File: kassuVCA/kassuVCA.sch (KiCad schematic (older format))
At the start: 20 parts, among them J1 Conn_02x05_Odd_Even, Q1 2N3904, Q2 2N3904, Q3 2N3904, U1 TL072

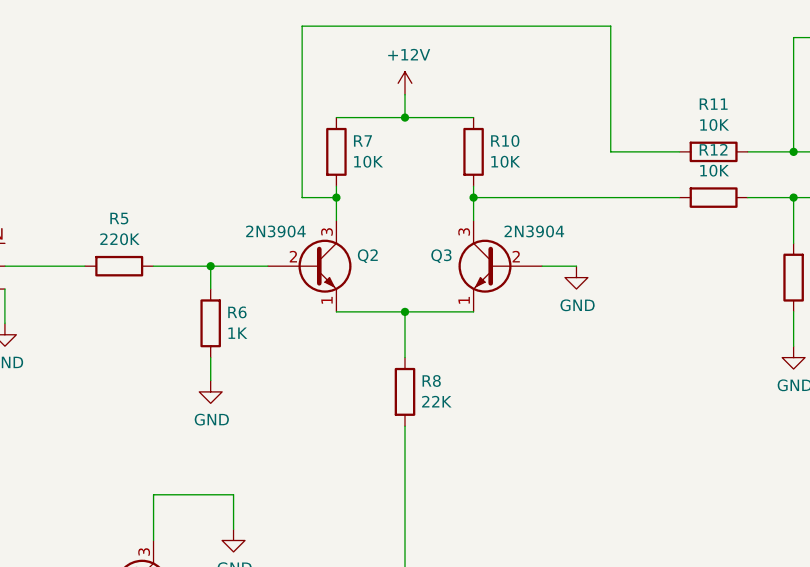
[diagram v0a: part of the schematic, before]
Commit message: switch to mbt3904 double transistor 2n3904 dual package
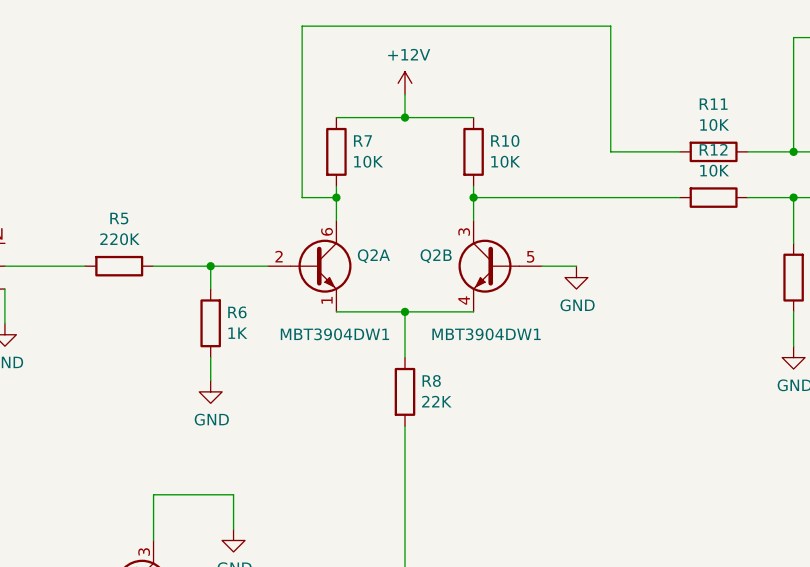
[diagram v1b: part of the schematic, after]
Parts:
- removed Q2, Q3: 2N3904, Package_TO_SOT_THT:TO-92L_Inline_Wide, symbol Transistor_BJT:2N3904
- added Q2: MBT3904DW1, Package_TO_SOT_SMD:SOT-363_SC-70-6, symbol Transistor_BJT:MBT3904DW1
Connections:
- net GND: now also Q2.5 (B2)
- net at R8.1: now also Q2.1 (E1), Q2.4 (E2)
- net at R5.1, R6.2: now also Q2.2 (B1)
- net at R11.2, R7.2: now also Q2.6 (C1)
- net at R10.2, R12.2: now also Q2.3 (C2)
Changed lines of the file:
@@
 $EndDescr
-$Comp
-L Transistor_BJT:2N3904 Q2
-U 1 1 622D83A3
-P 4100 2200
-F 0 "Q2" H 4290 2246 50  0000 L CNN
-F 1 "2N3904" H 3800 2350 50  0000 L CNN
-F 2 "Package_TO_SOT_THT:TO-92L_Inline_Wide" H 4300 2125 50  0001 L CIN
-F 3 "https://www.onsemi.com/pub/Collateral/2N3903-D.PDF" H 4100 2200 50  0001 L CNN
-	1    4100 2200
-	1    0    0    -1
-$EndComp
-$Comp
-L Transistor_BJT:2N3904 Q3
-U 1 1 622D8CF8
-P 4900 2200
-F 0 "Q3" H 5091 2246 50  0000 L CNN
-F 1 "2N3904" H 4600 2350 50  0000 L CNN
-F 2 "Package_TO_SOT_THT:TO-92L_Inline_Wide" H 5100 2125 50  0001 L CIN
-F 3 "https://www.onsemi.com/pub/Collateral/2N3903-D.PDF" H 4900 2200 50  0001 L CNN
-	1    4900 2200
-	-1   0    0    -1
-$EndComp
 $Comp
 L Transistor_BJT:2N3904 Q1
@@
 	1    0    0    -1
 $EndComp
+$Comp
+L Transistor_BJT:MBT3904DW1 Q2
+U 1 1 6229C328
+P 4100 2200
+F 0 "Q2" H 4290 2246 50  0000 L CNN
+F 1 "MBT3904DW1" H 3950 1900 50  0000 L CNN
+F 2 "Package_TO_SOT_SMD:SOT-363_SC-70-6" H 4300 2300 50  0001 C CNN
+F 3 "http://www.onsemi.com/pub_link/Collateral/MBT3904DW1T1-D.PDF" H 4100 2200 50  0001 C CNN
+	1    4100 2200
+	1    0    0    -1
+$EndComp
+$Comp
+L Transistor_BJT:MBT3904DW1 Q2
+U 2 1 6229CF49
+P 4900 2200
+F 0 "Q2" H 5091 2246 50  0000 L CNN
+F 1 "MBT3904DW1" H 4700 1900 50  0000 L CNN
+F 2 "Package_TO_SOT_SMD:SOT-363_SC-70-6" H 5100 2300 50  0001 C CNN
+F 3 "http://www.onsemi.com/pub_link/Collateral/MBT3904DW1T1-D.PDF" H 4900 2200 50  0001 C CNN
+	2    4900 2200
+	-1   0    0    -1
+$EndComp
 $EndSCHEMATC

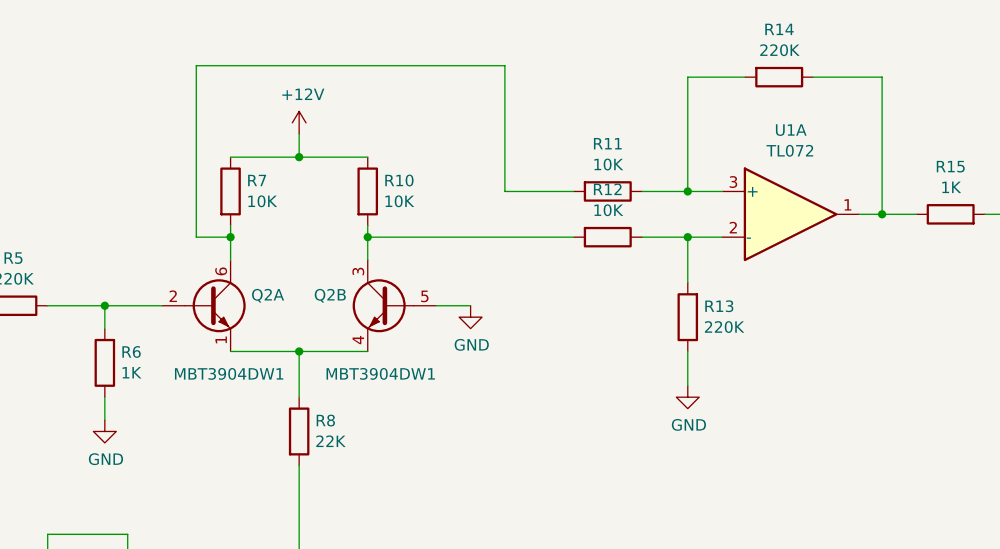
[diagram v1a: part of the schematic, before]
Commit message: VCA state working with jelly bean 2n3904 transistors
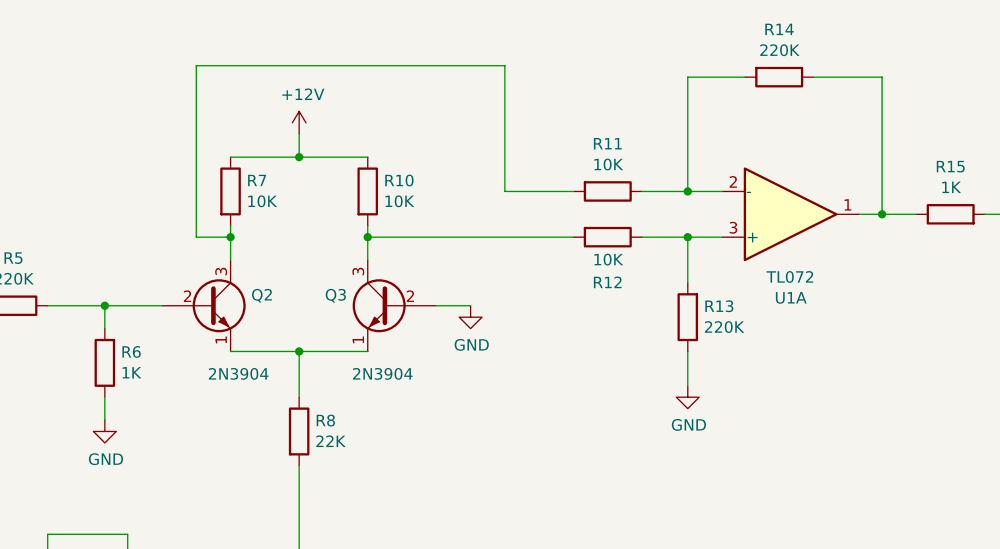
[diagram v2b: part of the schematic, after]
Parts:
- removed Q2: MBT3904DW1, Package_TO_SOT_SMD:SOT-363_SC-70-6, symbol Transistor_BJT:MBT3904DW1
- added Q2, Q3: 2N3904, Package_TO_SOT_THT:TO-92L_Inline_Wide, symbol Transistor_BJT:2N3904
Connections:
- net GND: now also Q3.2 (B)
- net at R12.1, R13.2: now also U1.3 (+); no longer U1.2 (-)
- net at R11.1, R14.2: now also U1.2 (-); no longer U1.3 (+)
- net at R8.1: now also Q2.1 (E), Q3.1 (E)
- net at R5.1, R6.2: now also Q2.2 (B)
- net at R11.2, R7.2: now also Q2.3 (C)
- net at R10.2, R12.2: now also Q3.3 (C)
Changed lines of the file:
@@
 	4500 2600 4500 2400
 Connection ~ 4500 2400
-Wire Wire Line
-	4500 2400 4800 2400
 $Comp
 L power:GND #PWR0106
@@
 U 1 1 62321712
 P 5850 1900
-F 0 "R12" V 5643 1900 50  0000 C CNN
-F 1 "10K" V 5734 1900 50  0000 C CNN
+F 0 "R12" V 6050 1900 50  0000 C CNN
+F 1 "10K" V 5950 1900 50  0000 C CNN
 F 2 "Resistor_THT:R_Axial_DIN0207_L6.3mm_D2.5mm_P10.16mm_Horizontal" V 5780 1900 50  0001 C CNN
 F 3 "~" H 5850 1900 50  0001 C CNN
@@
 F 3 "http://www.ti.com/lit/ds/symlink/tl071.pdf" H 6650 1800 50  0001 C CNN
 	1    6650 1800
-	1    0    0    -1
+	1    0    0    1
 $EndComp
 $Comp
@@
 $EndComp
 $Comp
-L Transistor_BJT:MBT3904DW1 Q2
-U 1 1 6229C328
+L Transistor_BJT:2N3904 Q2
+U 1 1 623E074C
 P 4100 2200
 F 0 "Q2" H 4290 2246 50  0000 L CNN
-F 1 "MBT3904DW1" H 3950 1900 50  0000 L CNN
-F 2 "Package_TO_SOT_SMD:SOT-363_SC-70-6" H 4300 2300 50  0001 C CNN
-F 3 "http://www.onsemi.com/pub_link/Collateral/MBT3904DW1T1-D.PDF" H 4100 2200 50  0001 C CNN
+F 1 "2N3904" H 4100 1900 50  0000 L CNN
+F 2 "Package_TO_SOT_THT:TO-92L_Inline_Wide" H 4300 2125 50  0001 L CIN
+F 3 "https://www.onsemi.com/pub/Collateral/2N3903-D.PDF" H 4100 2200 50  0001 L CNN
 	1    4100 2200
 	1    0    0    -1
 $EndComp
 $Comp
-L Transistor_BJT:MBT3904DW1 Q2
-U 2 1 6229CF49
+L Transistor_BJT:2N3904 Q3
+U 1 1 623E0DE4
 P 4900 2200
-F 0 "Q2" H 5091 2246 50  0000 L CNN
-F 1 "MBT3904DW1" H 4700 1900 50  0000 L CNN
-F 2 "Package_TO_SOT_SMD:SOT-363_SC-70-6" H 5100 2300 50  0001 C CNN
-F 3 "http://www.onsemi.com/pub_link/Collateral/MBT3904DW1T1-D.PDF" H 4900 2200 50  0001 C CNN
-	2    4900 2200
+F 0 "Q3" H 5090 2246 50  0000 L CNN
+F 1 "2N3904" H 4800 1900 50  0000 L CNN
+F 2 "Package_TO_SOT_THT:TO-92L_Inline_Wide" H 5100 2125 50  0001 L CIN
+F 3 "https://www.onsemi.com/pub/Collateral/2N3903-D.PDF" H 4900 2200 50  0001 L CNN
+	1    4900 2200
 	-1   0    0    -1
 $EndComp
+Wire Wire Line
+	4500 2400 4800 2400
 $EndSCHEMATC

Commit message: mini transistor success!
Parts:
- removed Q2, Q3: 2N3904, Package_TO_SOT_THT:TO-92L_Inline_Wide, symbol Transistor_BJT:2N3904
- added Q2: MBT3904DW1, Package_TO_SOT_SMD:SOT-363_SC-70-6, symbol Transistor_BJT:MBT3904DW1
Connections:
- net GND: now also Q2.5 (B2)
- net at R11.2, R7.2: now also Q2.6 (C1)
- net at R10.2, R12.2: now also Q2.3 (C2)
- net at R8.1: now also Q2.1 (E1), Q2.4 (E2)
- net at R5.1, R6.2: now also Q2.2 (B1)
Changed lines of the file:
@@
 	1    0    0    -1
 $EndComp
+Wire Wire Line
+	4500 2400 4800 2400
 $Comp
-L Transistor_BJT:2N3904 Q2
-U 1 1 623E074C
+L Transistor_BJT:MBT3904DW1 Q2
+U 1 1 624028ED
 P 4100 2200
 F 0 "Q2" H 4290 2246 50  0000 L CNN
-F 1 "2N3904" H 4100 1900 50  0000 L CNN
-F 2 "Package_TO_SOT_THT:TO-92L_Inline_Wide" H 4300 2125 50  0001 L CIN
-F 3 "https://www.onsemi.com/pub/Collateral/2N3903-D.PDF" H 4100 2200 50  0001 L CNN
+F 1 "MBT3904DW1" H 3950 1900 50  0000 L CNN
+F 2 "Package_TO_SOT_SMD:SOT-363_SC-70-6" H 4300 2300 50  0001 C CNN
+F 3 "http://www.onsemi.com/pub_link/Collateral/MBT3904DW1T1-D.PDF" H 4100 2200 50  0001 C CNN
 	1    4100 2200
 	1    0    0    -1
 $EndComp
 $Comp
-L Transistor_BJT:2N3904 Q3
-U 1 1 623E0DE4
+L Transistor_BJT:MBT3904DW1 Q2
+U 2 1 62403809
 P 4900 2200
-F 0 "Q3" H 5090 2246 50  0000 L CNN
-F 1 "2N3904" H 4800 1900 50  0000 L CNN
-F 2 "Package_TO_SOT_THT:TO-92L_Inline_Wide" H 5100 2125 50  0001 L CIN
-F 3 "https://www.onsemi.com/pub/Collateral/2N3903-D.PDF" H 4900 2200 50  0001 L CNN
-	1    4900 2200
+F 0 "Q2" H 5091 2246 50  0000 L CNN
+F 1 "MBT3904DW1" H 4700 1900 50  0000 L CNN
+F 2 "Package_TO_SOT_SMD:SOT-363_SC-70-6" H 5100 2300 50  0001 C CNN
+F 3 "http://www.onsemi.com/pub_link/Collateral/MBT3904DW1T1-D.PDF" H 4900 2200 50  0001 C CNN
+	2    4900 2200
 	-1   0    0    -1
 $EndComp
-Wire Wire Line
-	4500 2400 4800 2400
 $EndSCHEMATC

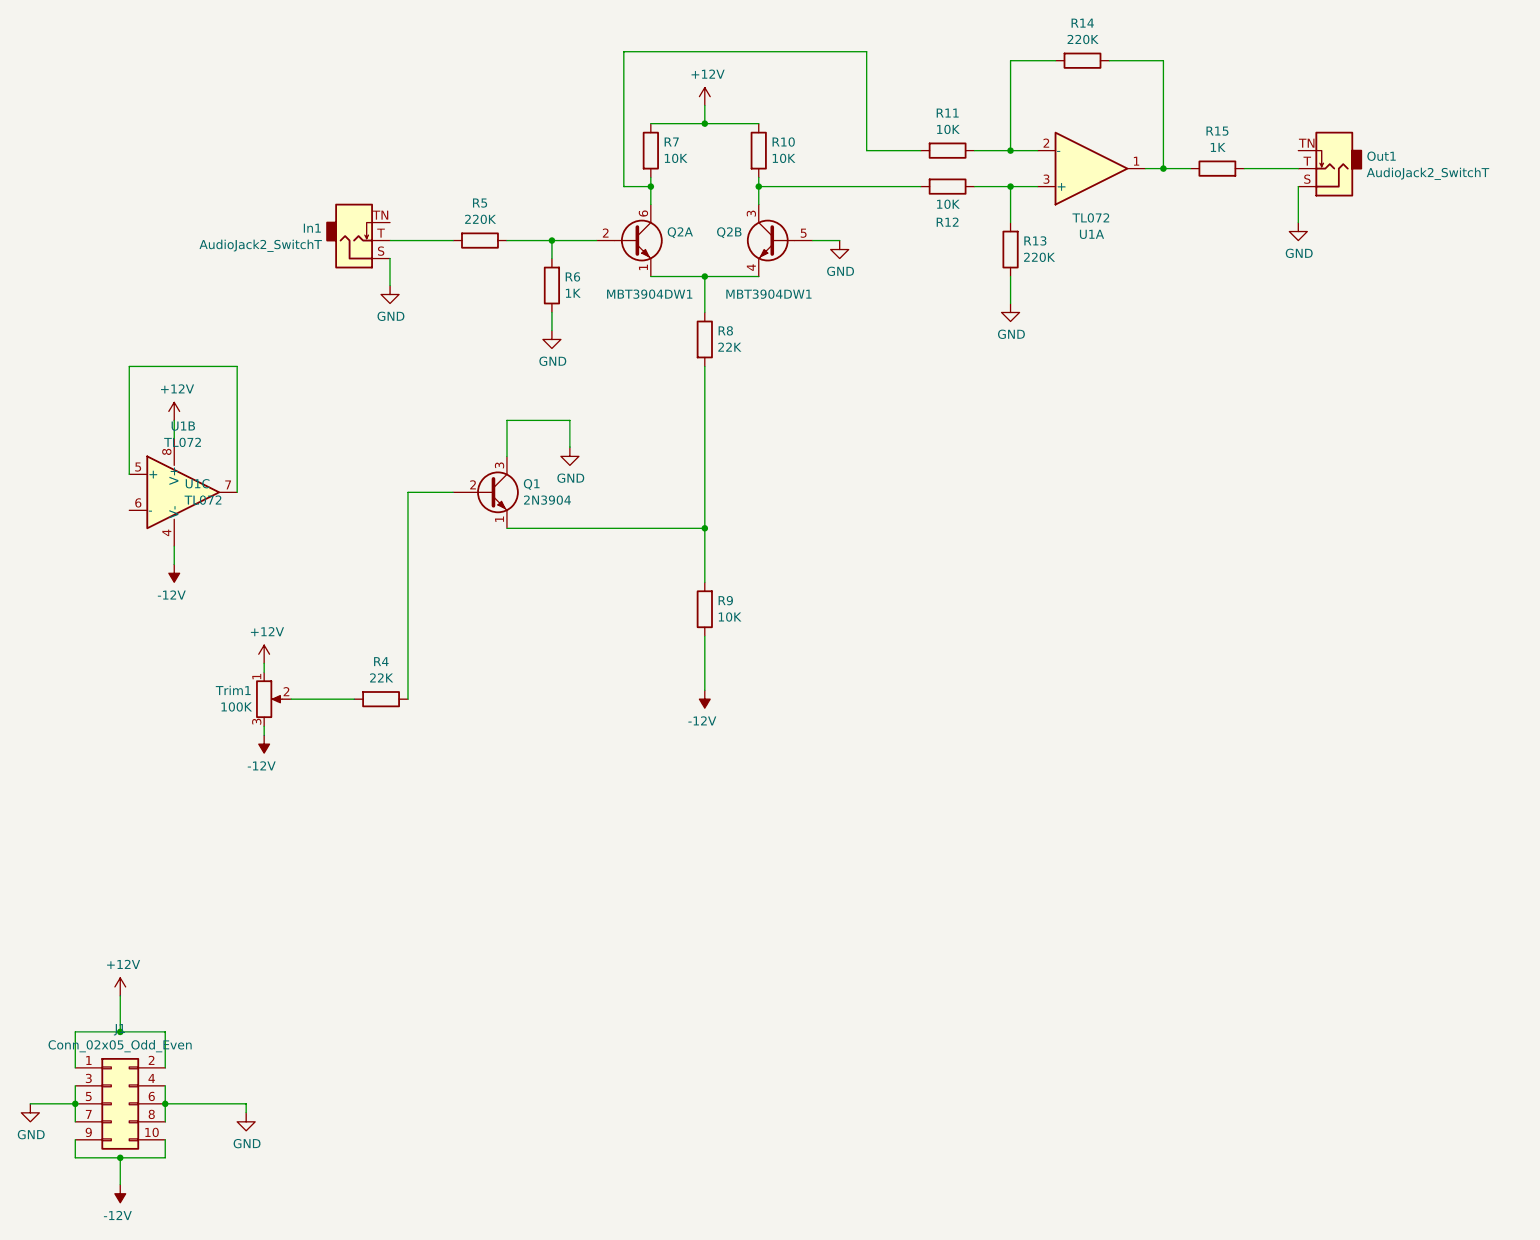
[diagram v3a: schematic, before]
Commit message: WIP working towards a mixer
2 channels laid out with 207 resistors and TL074s. I need to move to TL072s and monolithic transistors in a few places for saner routing
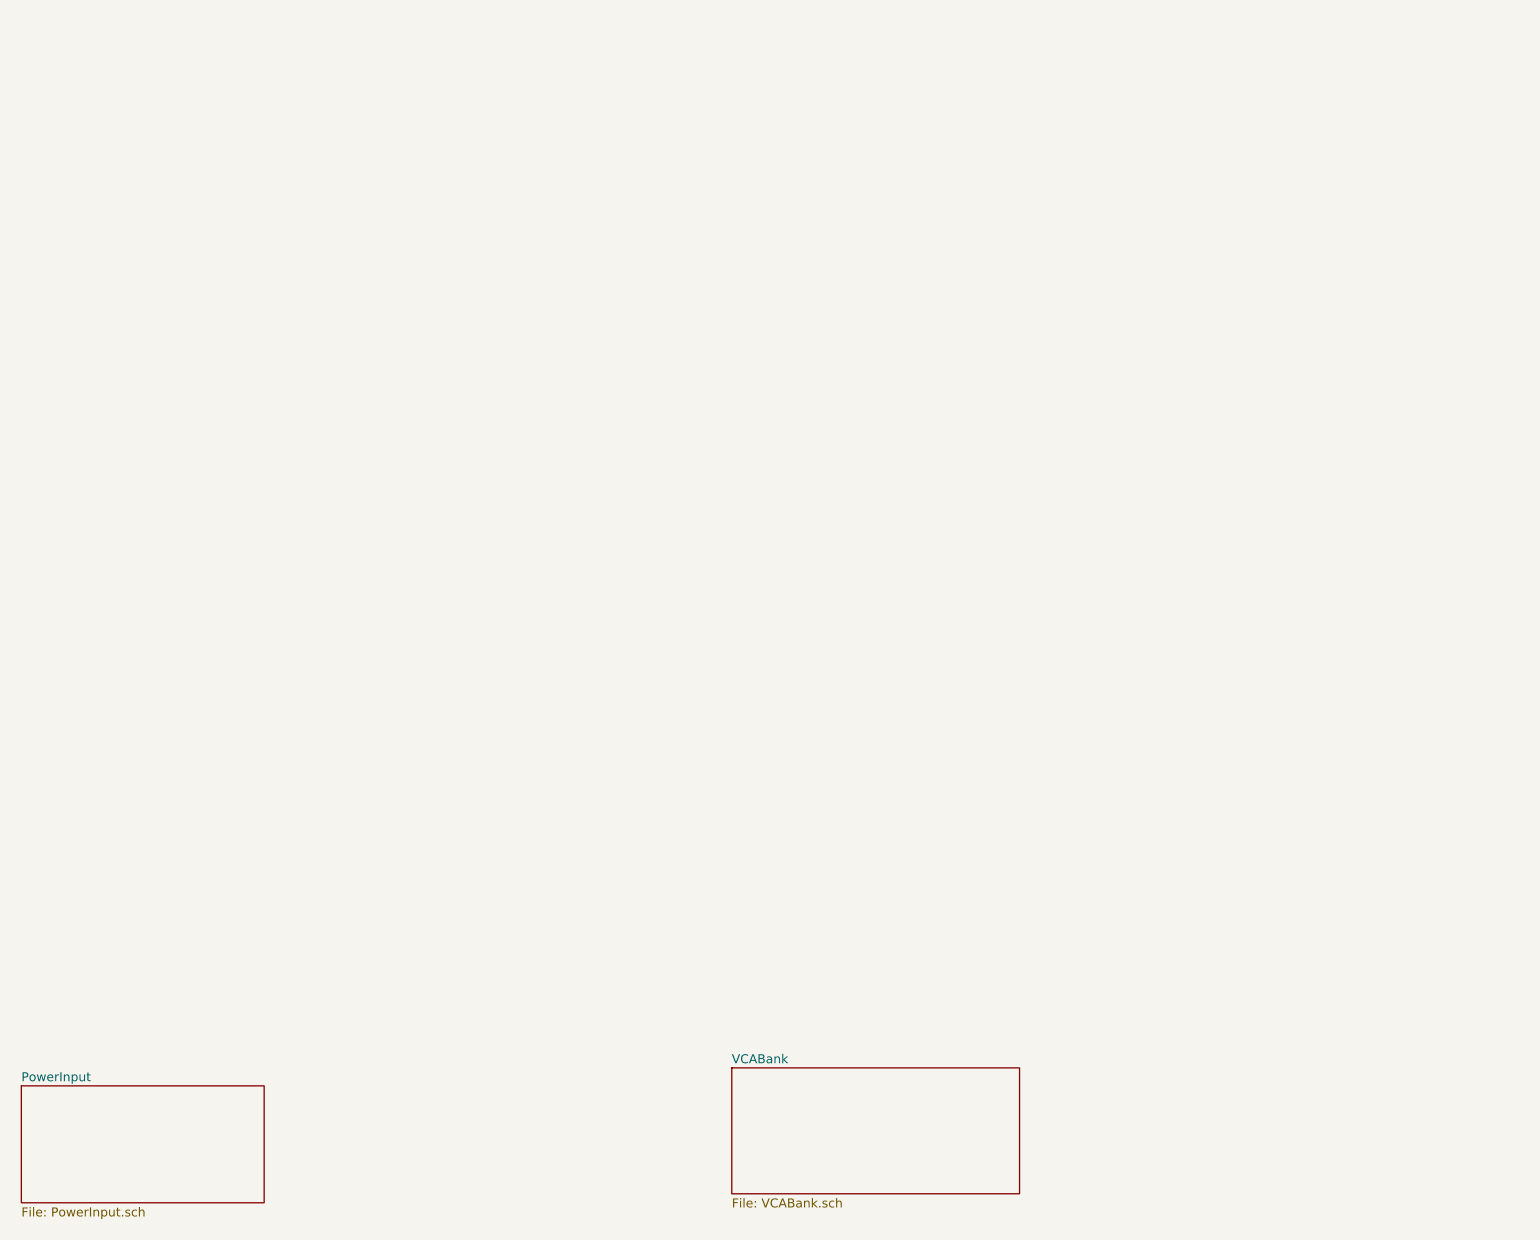
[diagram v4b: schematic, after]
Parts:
- removed In1, Out1: AudioJack2_SwitchT, Connector_Audio:Jack_3.5mm_QingPu_WQP-PJ398SM_Vertical_CircularHoles, symbol Connector:AudioJack2_SwitchT
- removed J1: Conn_02x05_Odd_Even, Connector_PinHeader_2.54mm:PinHeader_2x05_P2.54mm_Vertical, symbol Connector_Generic:Conn_02x05_Odd_Even
- removed Q1: 2N3904, Package_TO_SOT_THT:TO-92L_Inline_Wide, symbol Transistor_BJT:2N3904
- removed Q2: MBT3904DW1, Package_TO_SOT_SMD:SOT-363_SC-70-6, symbol Transistor_BJT:MBT3904DW1
- removed R10, R11, R12, R7, R9: 10K, Resistor_THT:R_Axial_DIN0207_L6.3mm_D2.5mm_P10.16mm_Horizontal, symbol Device:R
- removed R13, R14, R5: 220K, Resistor_THT:R_Axial_DIN0207_L6.3mm_D2.5mm_P10.16mm_Horizontal, symbol Device:R
- removed R15, R6: 1K, Resistor_THT:R_Axial_DIN0207_L6.3mm_D2.5mm_P10.16mm_Horizontal, symbol Device:R
- removed R4, R8: 22K, Resistor_THT:R_Axial_DIN0207_L6.3mm_D2.5mm_P10.16mm_Horizontal, symbol Device:R
- removed Trim1: 100K, Potentiometer_THT:Potentiometer_Alps_RK09K_Single_Vertical, symbol Device:R_POT
- removed U1: TL072, Package_DIP:DIP-8_W7.62mm_LongPads, symbol Amplifier_Operational:TL072
